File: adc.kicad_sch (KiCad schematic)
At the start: 56 parts, among them U1 MCP3008, U2 MCP6004, U3 MCP6004

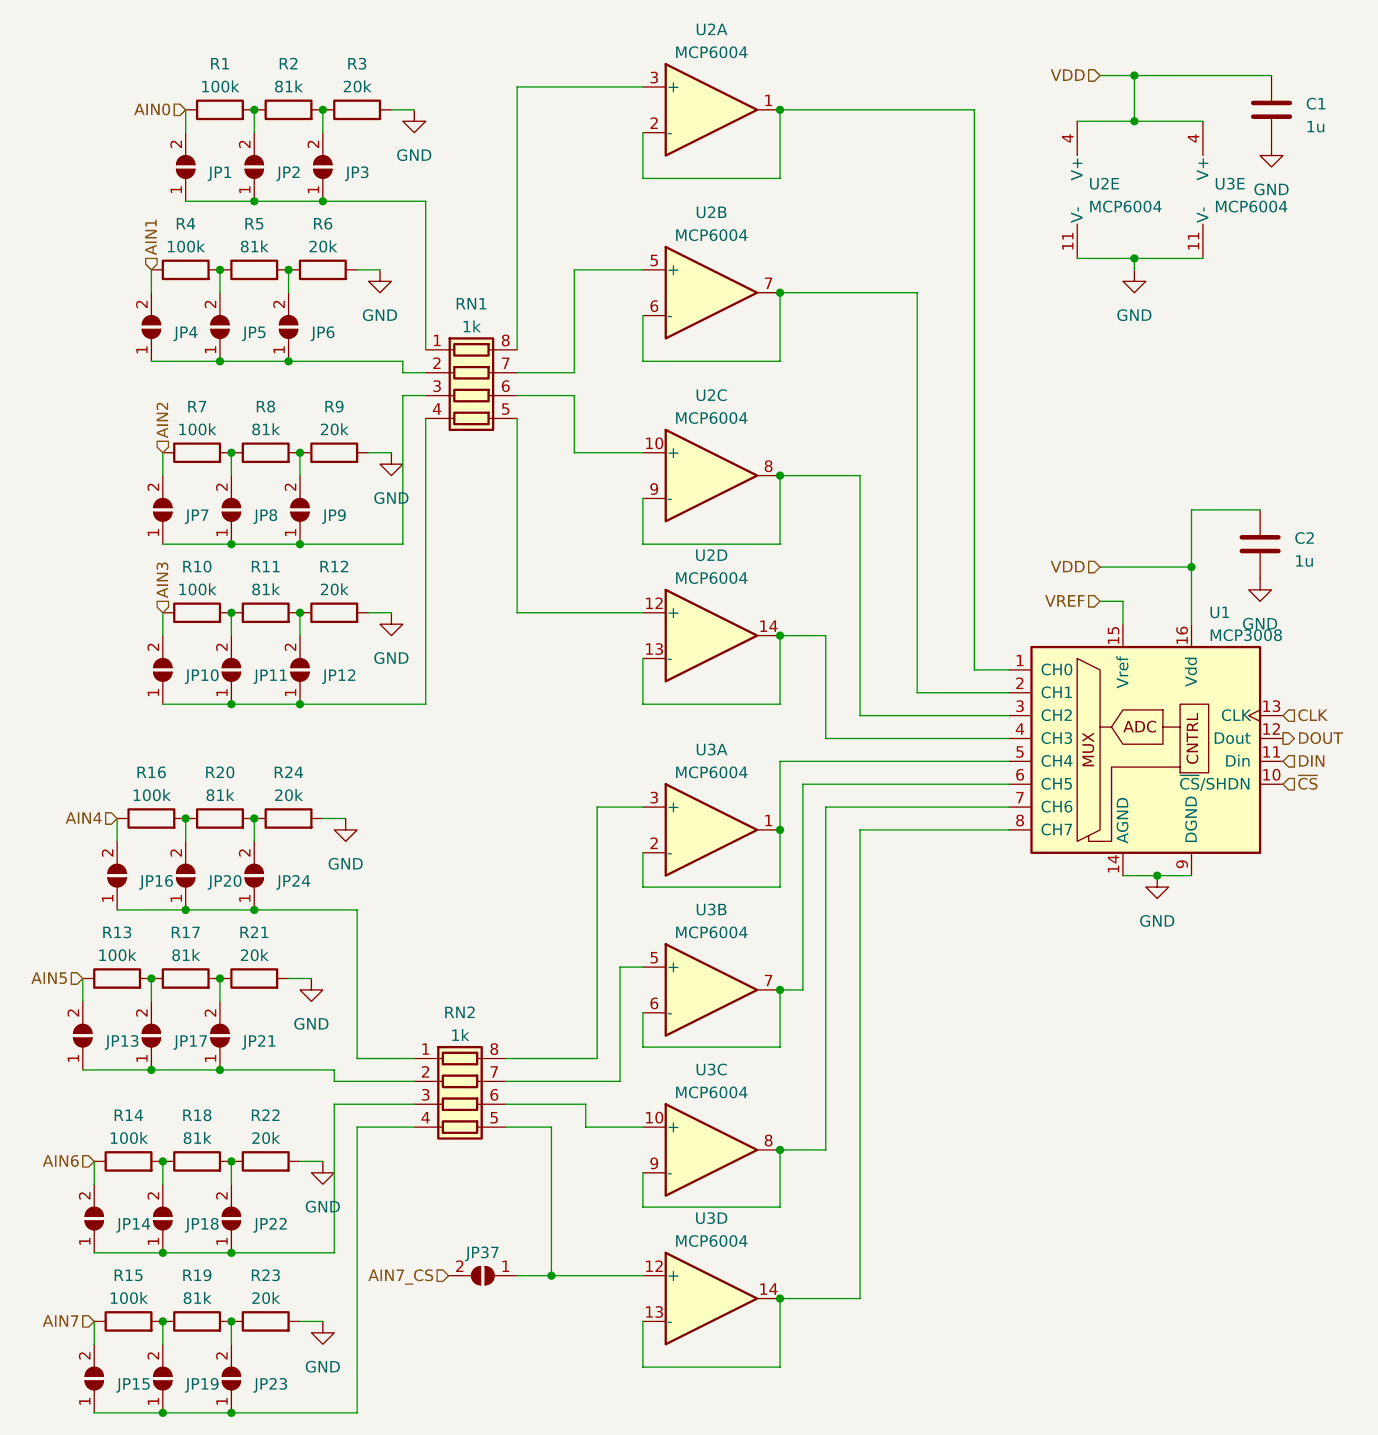
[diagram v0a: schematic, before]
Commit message: Build pogoplayground v1.0 - Fix continuity tester reference voltage - Fix SSR 5V supply
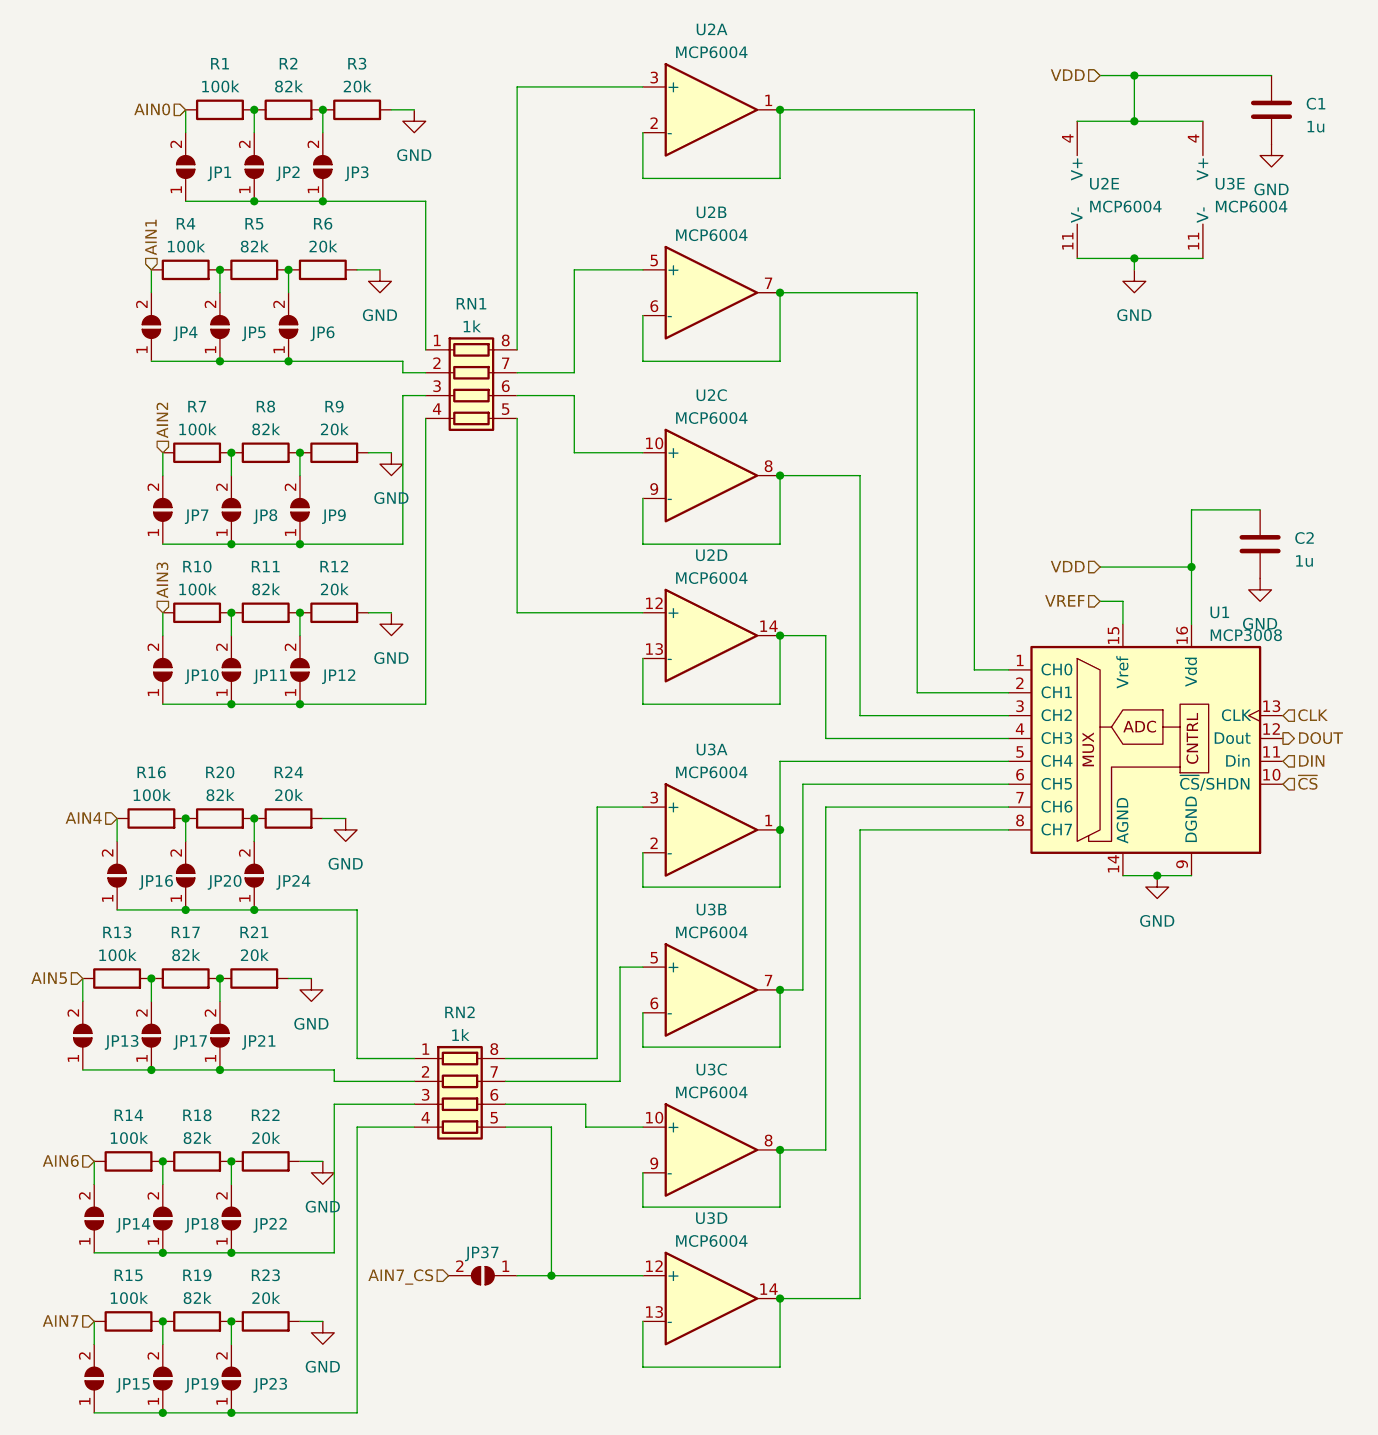
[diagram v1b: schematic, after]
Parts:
- R11, R17, R18, R19, R2, R20, R5, R8: value 81k -> 82k
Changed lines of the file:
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@@
       (effects (font (size 1.27 1.27)))
     )
-    (property "Value" "81k" (at 80.01 162.56 90)
+    (property "Value" "82k" (at 80.01 162.56 90)
       (effects (font (size 1.27 1.27)))
     )
@@
       (effects (font (size 1.27 1.27)))
     )
-    (property "Value" "81k" (at 82.55 106.68 90)
+    (property "Value" "82k" (at 82.55 106.68 90)
       (effects (font (size 1.27 1.27)))
     )
@@
       (effects (font (size 1.27 1.27)))
     )
-    (property "Value" "81k" (at 80.01 144.78 90)
+    (property "Value" "82k" (at 80.01 144.78 90)
       (effects (font (size 1.27 1.27)))
     )
@@
       (effects (font (size 1.27 1.27)))
     )
-    (property "Value" "81k" (at 87.63 66.04 90)
+    (property "Value" "82k" (at 87.63 66.04 90)
       (effects (font (size 1.27 1.27)))
     )
@@
       (effects (font (size 1.27 1.27)))
     )
-    (property "Value" "81k" (at 87.63 83.82 90)
+    (property "Value" "82k" (at 87.63 83.82 90)
       (effects (font (size 1.27 1.27)))
     )
@@
       (effects (font (size 1.27 1.27)))
     )
-    (property "Value" "81k" (at 86.36 45.72 90)
+    (property "Value" "82k" (at 86.36 45.72 90)
       (effects (font (size 1.27 1.27)))
     )
@@
       (effects (font (size 1.27 1.27)))
     )
-    (property "Value" "81k" (at 90.17 27.94 90)
+    (property "Value" "82k" (at 90.17 27.94 90)
       (effects (font (size 1.27 1.27)))
     )
@@
       (effects (font (size 1.27 1.27)))
     )
-    (property "Value" "81k" (at 78.74 124.46 90)
-      (effects (font (size 1.27 1.27)))
-    )
+    (property "Value" "82k" (at 78.74 124.46 90)
+      (effects (font (size 1.27 1.27)))
+    )
